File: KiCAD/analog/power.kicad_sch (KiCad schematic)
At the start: 35 parts, among them J33 Screw_Terminal_01x02, J34 Screw_Terminal_01x02, J5 Screw_Terminal_01x02, K5 G6RL-1-DC12, K6 G6RL-1-DC12, U13 MCP1700x-330xxTO, U6 LM2940CT-5.0, U7 LT1054, U8 LM2940CT-12

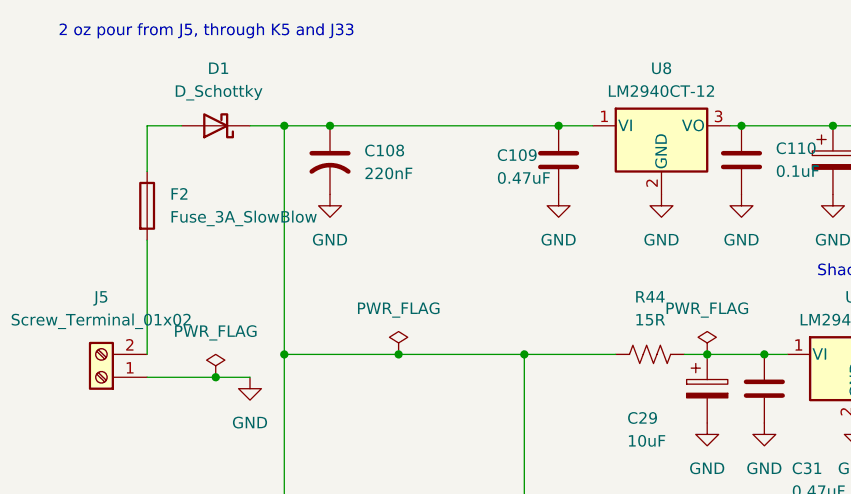
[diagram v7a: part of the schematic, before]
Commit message: revD: footprint pass across all boards + ss_pa fault-chain fix + LLM review brief
- New tools/assign_misc_footprints.py: lib_id-keyed footprint assigner
  (resistors, screw terminals, pin headers, LT1054); mirrors cap-script
  safe-write (UTF-8 no BOM, no CRLF translation).
- tools/assign_cap_footprints.py: added 0.47uF -> C_Rect_L7.0mm case.
- Ran both scripts across analog, ss_pa, Output LPF, frontpanel,
  protoshield, and shelved power board. ~100 fills; details in diffs.
- ss_pa: R1-R4 (0.22 ohm source sense) upgraded to 2W Yageo RSF200
  with DIN0516 L15.5mm/P20.32mm footprint; Value tagged "0.22R 2W".
  R15/R16 confirmed 1/4W (DIN0207) for BS170 source degeneration.
- analog/power: R44 15R 5W horizontal, P30.48mm footprint.
- ss_pa fault chain (from external LLM review): R21/R22 raised
  10K -> 100K to restore self-latching loop gain; new R26 = 100K
  across C12 so cap discharges between power cycles (reliable reset).
  R26 footprint pending.
- Documentation/revD_llm_review_brief.md: new, comprehensive system
  description for external LLM deep-dive (function, component values,
  power dissipation, design flaws). References all five board netlists.

Co-Authored-By: Claude Opus 4.7 <noreply@anthropic.com>
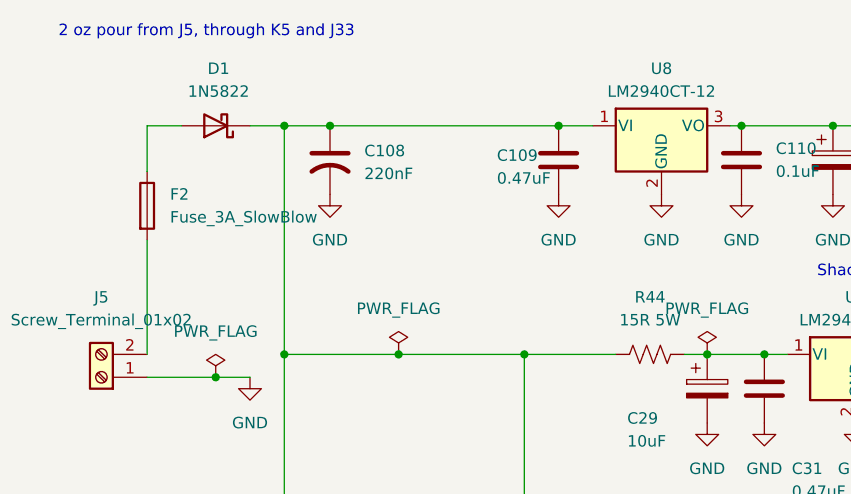
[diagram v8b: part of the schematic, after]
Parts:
- C29: footprint (none) -> Capacitor_THT:CP_Radial_D5.0mm_P2.00mm
- C31: footprint (none) -> Capacitor_THT:C_Rect_L7.0mm_W3.5mm_P5.00mm
- D1: value D_Schottky -> 1N5822
- R41, R42: footprint (none) -> Resistor_THT:R_Axial_DIN0207_L6.3mm_D2.5mm_P10.16mm_Horizontal
- R44: value 15R -> 15R 5W; footprint (none) -> Resistor_THT:R_Axial_Power_L25.0mm_W9.0mm_P30.48mm
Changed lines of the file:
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@@
 			)
 		)
-		(property "Footprint" ""
+		(property "Footprint" "Resistor_THT:R_Axial_DIN0207_L6.3mm_D2.5mm_P10.16mm_Horizontal"
 			(at 65.024 99.314 90)
 			(hide yes)
@@
 			)
 		)
-		(property "Footprint" ""
+		(property "Footprint" "Capacitor_THT:C_Rect_L7.0mm_W3.5mm_P5.00mm"
 			(at 152.0952 74.93 0)
 			(hide yes)
@@
 			)
 		)
-		(property "Value" "15R"
+		(property "Value" "15R 5W"
 			(at 138.43 63.5 90)
 			(show_name no)
@@
 			)
 		)
-		(property "Footprint" ""
+		(property "Footprint" "Resistor_THT:R_Axial_Power_L25.0mm_W9.0mm_P30.48mm"
 			(at 138.684 66.294 90)
 			(hide yes)
@@
 			)
 		)
-		(property "Footprint" ""
+		(property "Footprint" "Resistor_THT:R_Axial_DIN0207_L6.3mm_D2.5mm_P10.16mm_Horizontal"
 			(at 47.244 161.544 90)
 			(hide yes)
@@
 			)
 		)
-		(property "Value" "D_Schottky"
+		(property "Value" "1N5822"
 			(at 90.4875 38.1 0)
 			(show_name no)
@@
 			)
 		)
-		(property "Footprint" ""
+		(property "Footprint" "Capacitor_THT:CP_Radial_D5.0mm_P2.00mm"
 			(at 145.7452 74.93 0)
 			(hide yes)
